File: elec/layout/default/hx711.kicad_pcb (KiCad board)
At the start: 2 copper layers, 225.7 x 100.8 mm, 16 parts

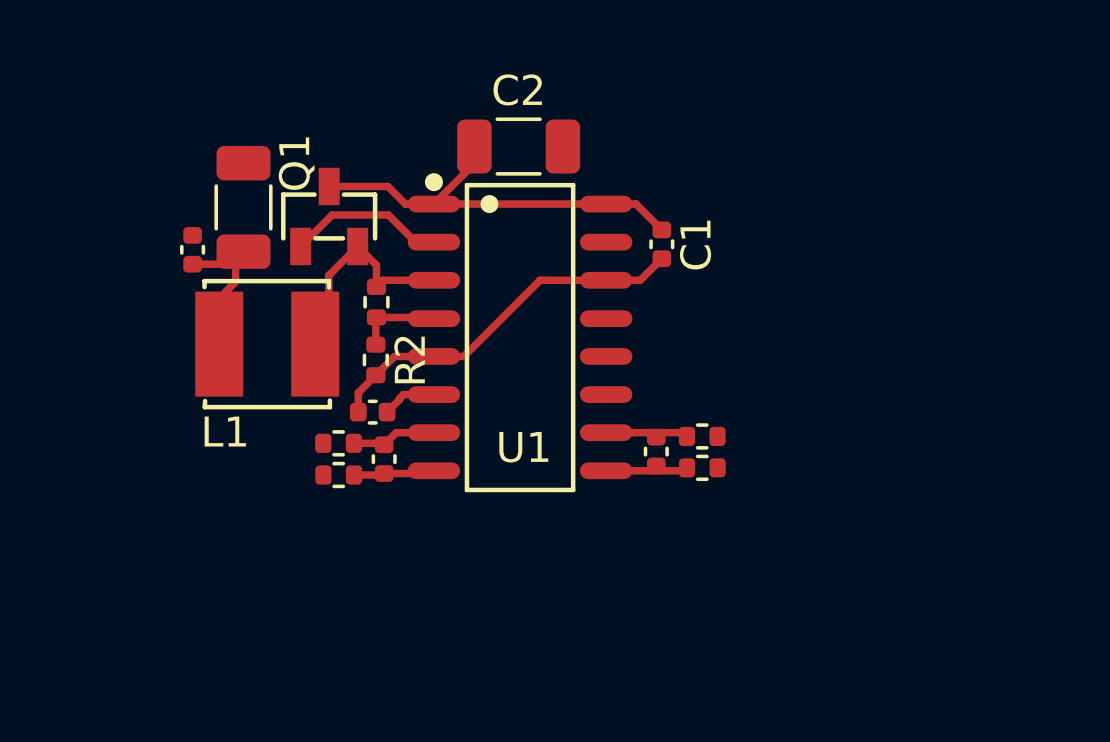
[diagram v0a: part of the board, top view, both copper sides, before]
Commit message: fixed emitter collector mixup
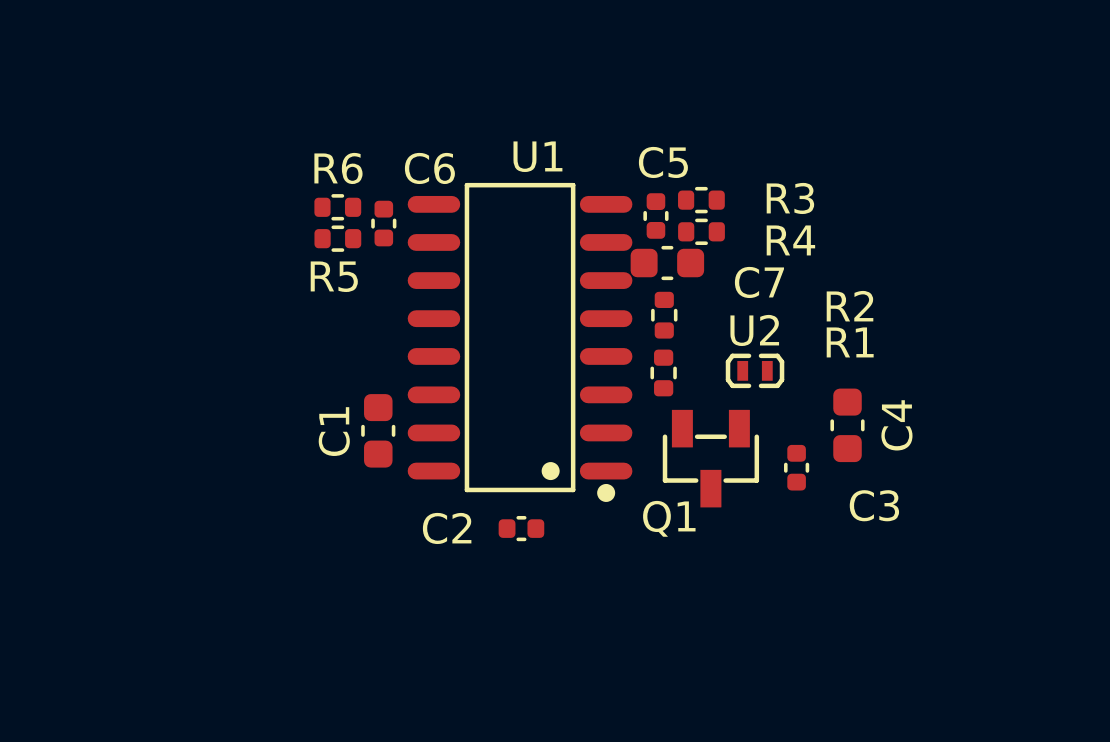
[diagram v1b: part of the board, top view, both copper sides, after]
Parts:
- removed L1: 1.23A 3.3uH ±20% SMD Power Inductors ROHS, lib:ato-04ea3db2-4b2f-45a6-9113-aa1f8beaa754
- added U2: 3.3 +/- 0.99 (30%) microhenry, lib:IND-SMD_L1.2-W0.7, F.Cu at (123.1, 48.7)
- C1, C4, C7: value Multilayer Ceramic Capacitors MLCC - SMD/SMT 100nF 10V 0402 RoHS -> 50V 100nF X7R ±10% 0603 Multilayer Ceramic Capacitors MLCC - SMD/SMT ROHS; footprint lib:C0402 -> lib:C0603
- C2, C3: value Multilayer Ceramic Capacitors MLCC - SMD/SMT 10uF 16V 1206 RoHS -> 6.3V 10uF X5R ±20% 0402 Multilayer Ceramic Capacitors MLCC - SMD/SMT ROHS; footprint lib:C1206 -> lib:C0402
- C5, C6: value Multilayer Ceramic Capacitors MLCC - SMD/SMT 100nF 10V 0402 RoHS -> 16V 100nF X7R ±10% 0402 Multilayer Ceramic Capacitors MLCC - SMD/SMT ROHS
- R1: value Chip Resistor - Surface Mount 20KOhms ±5% 1/16W 0402 RoHS -> 62.5mW Thick Film Resistors ±100ppm/℃ ±1% 10kΩ 0402 Chip Resistor - Surface Mount ROHS
- R2: value Chip Resistor - Surface Mount 8.2KOhms ±5% 1/16W 0402 RoHS -> 62.5mW Thick Film Resistors ±100ppm/℃ ±1% 8.2kΩ 0402 Chip Resistor - Surface Mount ROHS
- R3, R4, R5, R6: value Chip Resistor - Surface Mount 100Ohms ±5% 1/16W 0402 RoHS -> 62.5mW Thick Film Resistors ±1% ±200ppm/℃ 100Ω 0402 Chip Resistor - Surface Mount ROHS
- moved C4 22.6 mm to (126.2, 50.6), turned to -90 degrees
- moved C3 20.4 mm to (124.5, 52.0), turned to -90 degrees
- moved R3 15.2 mm to (121.3, 43.0), turned to 180 degrees
- moved Q1 15.1 mm to (121.6, 51.7), turned to 90 degrees
- moved R6 14.9 mm to (109.2, 43.3), turned to 180 degrees
- moved R4 14.0 mm to (121.3, 44.1), turned to 0 degrees
- moved R5 13.8 mm to (109.2, 44.3), turned to 0 degrees
- moved C2 12.7 mm to (115.3, 54.0), turned to 180 degrees
- moved C5 12.2 mm to (119.8, 43.6), turned to -90 degrees
- moved C6 11.8 mm to (110.7, 43.8), turned to 90 degrees
- moved C1 11.3 mm to (110.5, 50.7), turned to 90 degrees
- moved C7 11.0 mm to (120.2, 45.1), turned to 0 degrees
- moved R1 9.86 mm to (120.0, 48.8), turned to 90 degrees
- moved R2 9.73 mm to (120.0, 46.9), turned to 90 degrees
- turned U1 to 90 degrees
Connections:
- net avdd renamed ic-vcc-1
- net dout renamed data
- net pd_sck renamed clock
- C1 pad 1: vcc -> ic-vcc
- C2 pad 1: vcc -> ic-vcc
- C3 pad 1: vcc-1 -> vcc
- C3 pad 2: gnd-1 -> gnd
- C4 pad 1: vcc-1 -> vcc
- C4 pad 2: gnd-1 -> gnd
- Q1 pad 3: vcc -> ic-vcc
- R3 pad 2: inpa -> inna
- R4 pad 1: inna -> p
- R4 pad 2: p -> inpa
- R5 pad 2: inpb -> innb
- R6 pad 1: innb -> p-1
- R6 pad 2: p-1 -> inpb
- U1 pad 1: vcc -> ic-vcc
- U1 pad 16: vcc -> ic-vcc
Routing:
- net vcc: track 14.2 -> 0.00 mm
- net gnd: track 12.6 -> 0.00 mm
- net ic-vcc-1: track 7.45 -> 0.00 mm
- net vcc-1: track 5.29 -> 0.00 mm
- net base: track 5.25 -> 0.00 mm
- net inna: track 2.85 -> 0.00 mm
- net vfb: track 2.85 -> 0.00 mm
- net inpb: track 2.75 -> 0.00 mm
- net innb: track 2.74 -> 0.00 mm
- net inpa: track 2.72 -> 0.00 mm
- net vbg: track 1.83 -> 0.00 mm
